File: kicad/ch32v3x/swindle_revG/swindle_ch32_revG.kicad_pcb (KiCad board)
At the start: 2 copper layers, 49.8 x 33.3 mm, 65 parts, among them J1 jtag, J2 Conn_01x03_Socket, J2_DFU1 con2, J3 Debug port, J4 USB, J5 Debug port, U1 CH32V303RCT6, U2 LM1117-3.3, U3 3V->VTREF, U4 VTREF->3V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

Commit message: RP2040 : Add USE_RP2040 option to use the new PCB Kicad : RP2040 carrier layout mon : add mon enablereset to make exec from RAM work with vscode. That ignores the reset command sent by cortexdebug Misc : dont hardcode the target in the attach/vAttch command to 1.  Actually read the value.
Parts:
- removed the kibuzzard-65C1C789 at (114.7, 83.0)
- removed kibuzzard-65C1C7F5: G***, kibuzzard-65C1C7F5
- removed kibuzzard-65C1C805: G***, kibuzzard-65C1C805
- removed kibuzzard-6714B049: G***, kibuzzard-6714B049
- added kibuzzard-6731069B: G***, kibuzzard-6731069B, F.Cu at (115.0, 80.6)
- added kibuzzard-67310708: G***, kibuzzard-67310708, F.Cu at (114.9, 77.1)
- added kibuzzard-6731071F: G***, kibuzzard-6731071F, F.Cu at (114.9, 82.3)
- J3: value Debug port -> Dbg; footprint Connector_JST:JST_XH_B5B-XH-AM_1x05_P2.50mm_Vertical -> Connector_JST:JST_XH_B5B-XH-A_1x05_P2.50mm_Vertical
- U3, U4, U5: footprint Package_SO:VSSOP-8_2.3x2mm_P0.5mm -> Package_SO:TSSOP-8_3x3mm_P0.65mm
- moved RST1 4.81 mm to (131.6, 69.4)
- moved U6 4.51 mm to (122.8, 69.1)
- moved C10 3.99 mm to (117.8, 68.7), turned to 0 degrees
- moved R1 3.75 mm to (134.8, 76.1)
- moved J2_DFU1 3.11 mm to (135.3, 72.6), turned to 0 degrees
- moved C11 1.75 mm to (117.8, 70.3)
- moved U5 1.08 mm to (119.7, 73.0)
- moved kibuzzard-67137B47 0.80 mm to (114.9, 74.0)
- moved kibuzzard-671361D3 0.78 mm to (119.8, 82.9)
- moved U4 0.27 mm to (119.7, 80.6)
- moved kibuzzard-65C1C9D7 0.19 mm to (130.4, 72.4)
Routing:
- net +3.3V: track 179.6 -> 188.2 mm, vias 9 -> 11
- net V1.8: track 5.66 -> 11.3 mm, vias 0 -> 2
- net GND: track 274.3 -> 277.3 mm
- net VTREF: track 25.3 -> 22.7 mm
- net SWIO_DIR_3V: track 18.1 -> 20.6 mm
- net OUT_SWDCLK: track 22.3 -> 21.3 mm
- net INOUT_SWO: track 16.3 -> 15.4 mm
- net IN_FORCE_DFU: track 13.3 -> 13.8 mm

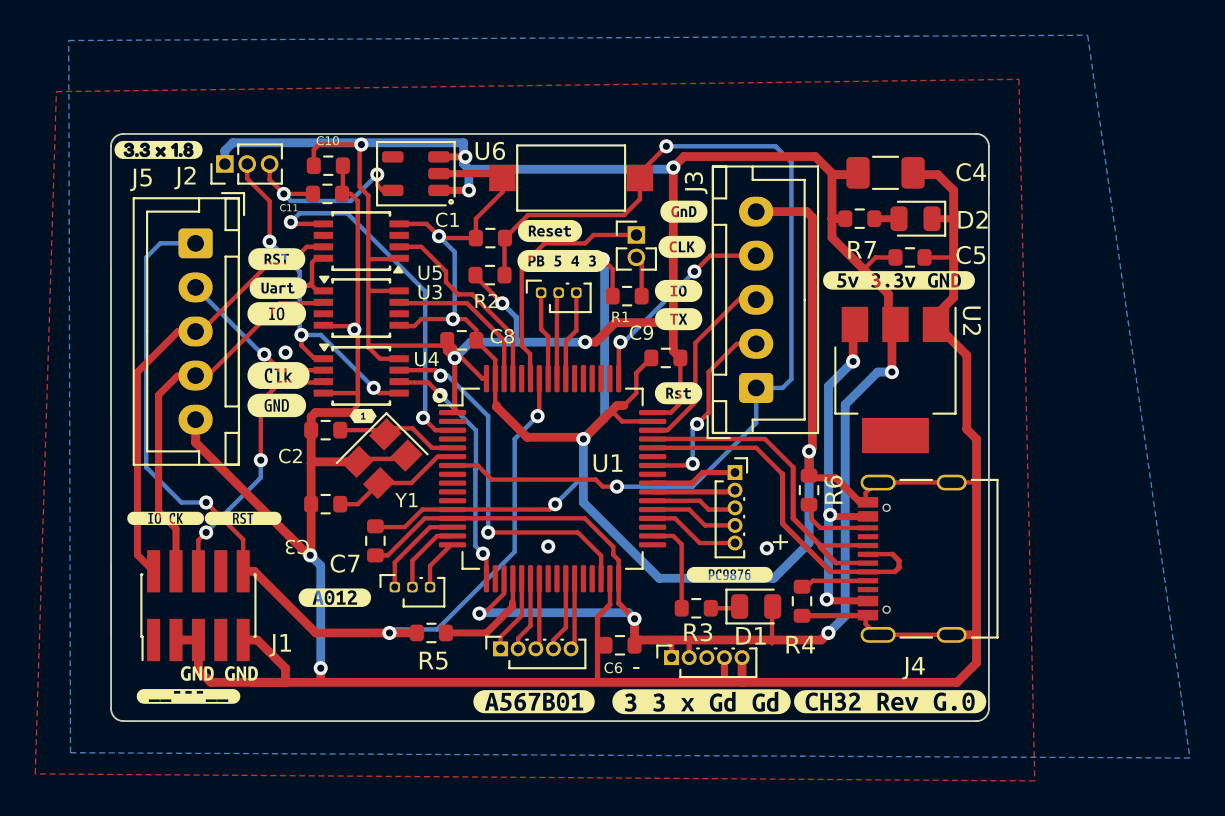
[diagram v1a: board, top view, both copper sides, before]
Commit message: kicad : use PC3 instead of PC14, which is not usable as GPIO on ch32v2/3
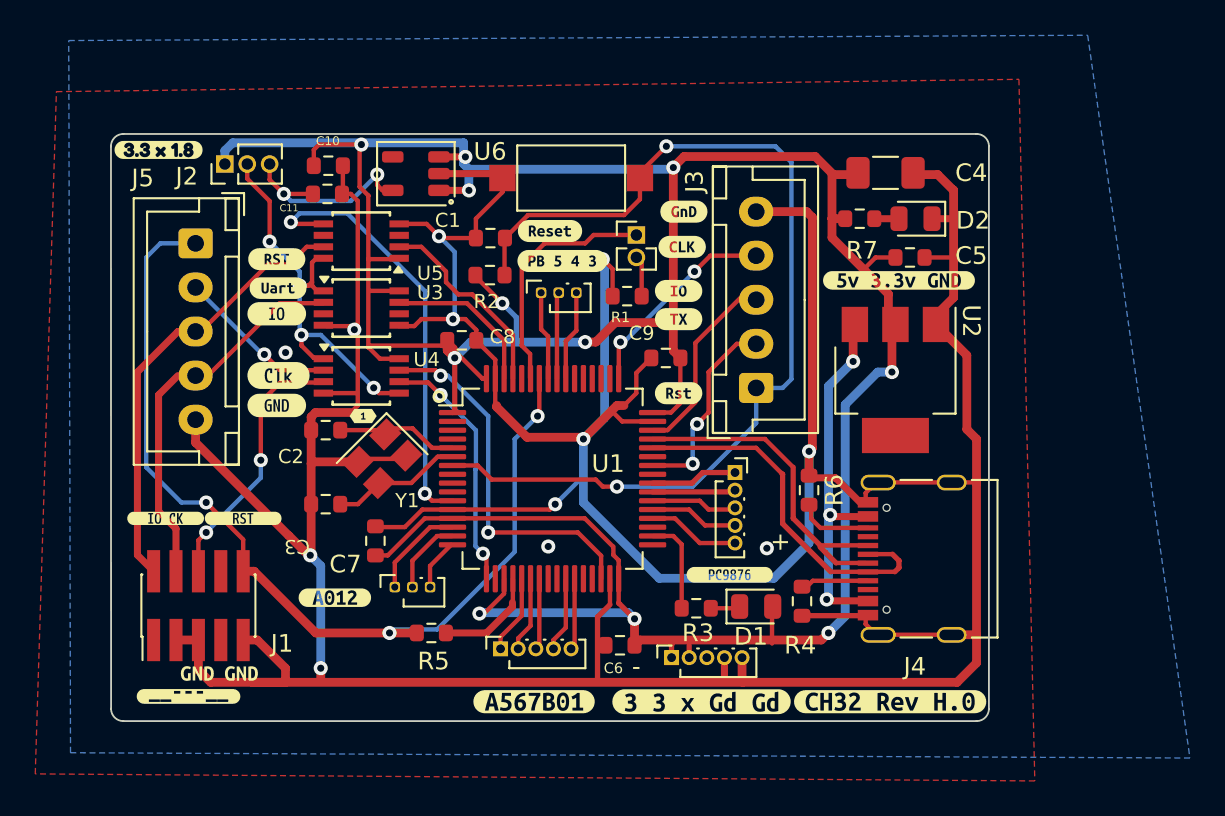
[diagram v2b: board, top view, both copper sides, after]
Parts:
- removed kibuzzard-6714FD63: G***, kibuzzard-6714FD63
- added kibuzzard-679335ED: G***, kibuzzard-679335ED, F.Cu at (149.7, 99.1)
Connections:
- U1 pad 11: unconnected-(U1-PC3-Pad11) -> SWIO_DIR_3V
- U1 pad 3: SWIO_DIR_3V -> unconnected-(U1-PC14-Pad3)
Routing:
- net SWIO_DIR_3V: track 20.6 -> 24.6 mm
